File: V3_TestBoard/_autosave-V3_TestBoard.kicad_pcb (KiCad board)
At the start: 2 copper layers, 157.2 x 180.9 mm, 42 parts, among them J1 DT/CK/EN, J10 Resistor Socket (2), J11 Pins 22->37, J12 Oscillator Connection Pins, J13 Oscillator Connection Pins, J14 Pins 21->5, J15 27&33/36 Jumper, J16 Resistor Socket (4), J17 Resistor Socket (3), J18 Ext_VCC_2v5 Header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

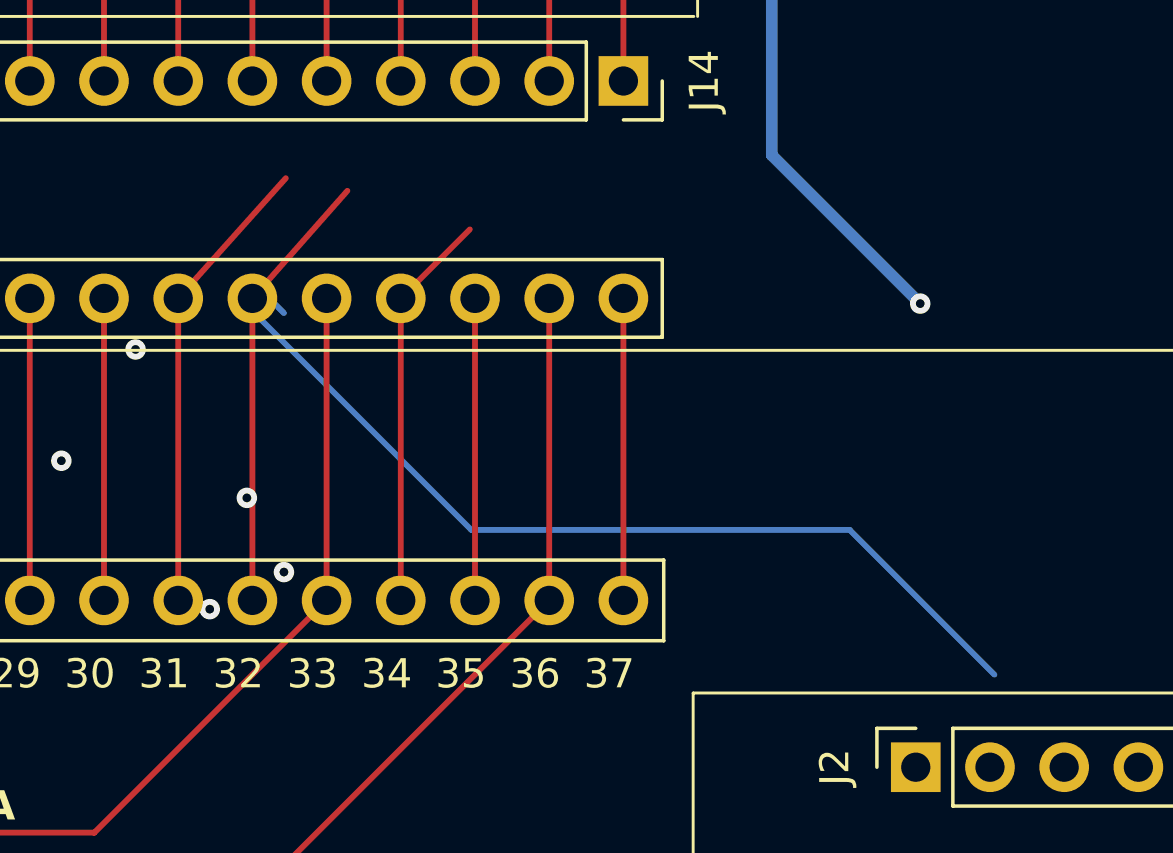
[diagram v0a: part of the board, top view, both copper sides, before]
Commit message: Updated V3_Motherboard to fab revision
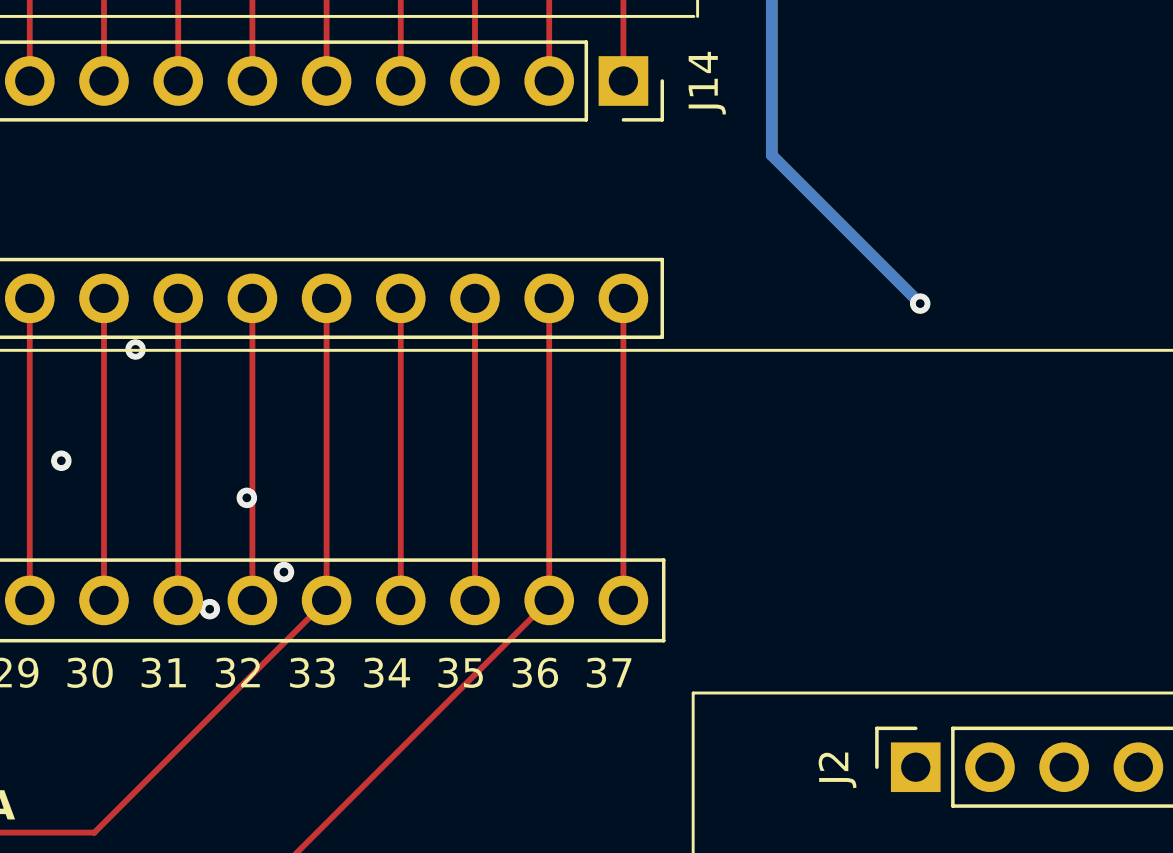
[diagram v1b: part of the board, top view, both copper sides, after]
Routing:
- net 32&56&VCC_3v3/2: track 70.0 -> 32.3 mm
- net 59&31->52&53: track 48.1 -> 42.5 mm
- net 34&55: track 23.7 -> 20.4 mm
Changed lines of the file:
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@@
-		(net 45)
-	)
-	(segment
-		(start 145.859 123.6012)
-		(end 149.1102 119.9182)
-		(width 0.2)
-		(layer "F.Cu")
 		(net 45)
 	)
@@
 	)
 	(segment
-		(start 171.259 136.479)
-		(end 166.306 131.526)
-		(width 0.2)
-		(layer "B.Cu")
-		(net 45)
-	)
-	(segment
 		(start 174.399 152.049)
 		(end 177.059 152.049)
@@
 	)
 	(segment
-		(start 146.939 124.104)
-		(end 145.788 122.953)
-		(width 0.2)
-		(layer "B.Cu")
-		(net 45)
-	)
-	(segment
-		(start 166.306 131.526)
-		(end 153.352 131.526)
-		(width 0.2)
-		(layer "B.Cu")
-		(net 45)
-	)
-	(segment
 		(start 174.399 154.589)
 		(end 174.399 152.049)
@@
 	)
 	(segment
-		(start 145.4272 123.6012)
-		(end 153.352 131.526)
-		(width 0.2)
-		(layer "B.Cu")
-		(net 45)
-	)
-	(segment
 		(start 252.539 133.859)
 		(end 252.539 123.859)
@@
 		(start 249.999 123.779)
 		(end 252.539 123.779)
-		(width 0.2)
-		(layer "F.Cu")
-		(net 46)
-	)
-	(segment
-		(start 143.319 123.6012)
-		(end 147.002 119.4864)
 		(width 0.2)
 		(layer "F.Cu")
@@
 		(width 0.2)
 		(layer "F.Cu")
-		(net 60)
-	)
-	(segment
-		(start 150.939 123.6012)
-		(end 153.3012 121.239)
-		(width 0.2)
-		(layer "F.Cu")
